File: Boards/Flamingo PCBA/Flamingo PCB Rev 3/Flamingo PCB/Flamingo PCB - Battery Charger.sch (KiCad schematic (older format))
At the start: 13 parts, among them J301 Wire Switch Here, J302 JST PH Battery Connector

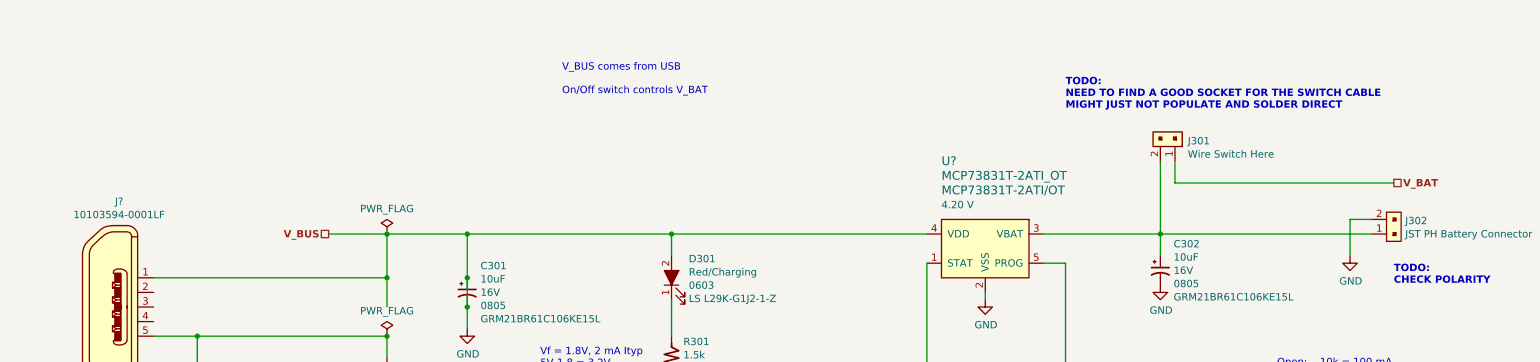
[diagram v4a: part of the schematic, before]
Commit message: NOSTUFF 5V LDO bc not needed. Added Sch diode on 5v LDO.
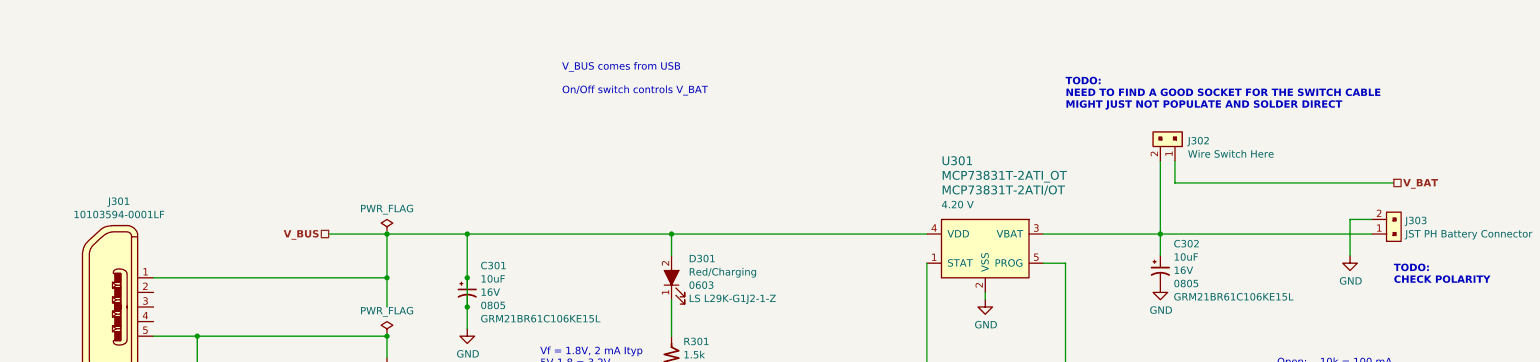
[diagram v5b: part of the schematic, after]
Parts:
- gave numbers to parts that had none: 2
- renumbered J301 to J302, J302 to J303
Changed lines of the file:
@@
 --------FLOW CHART--------\n\n###SHUTDOWN MODE\nVDD < VUVLO\nVDD < VBAT\nor\nPROG > 200 k\nSTAT = High Z\n\n###PRECONDITIONING \nCharge Current = IPREG\nSTAT = LOW\n\n###FAST CHARGE \nAlso get here if VBAT > VPTH from SHUTDOWN    \nor   \nVBAT < VRTH  from CHARGE COMPLETE\n\nCharge Current = IREG\nSTAT = LOW\n\n###CONSTANT VOLTAGE \nCharge Voltage = VREG\nSTAT = LOW\n\n###CHARGE MODE \nSTAT = HIGH (MCP73831)\nSTAT = High Z (MCP73832)\n\n--------PART NUMBER BREAKDOWN--------\n\nMCP73831T - 2 * * * _ OT\n\n(T) Tape and reel\n(2) 4.20 V regulated\n(OT) SMall Outline Transistor SOT23 T-Lead\n\n#######\n\nMCP73831T - 2 A C I _ OT\n(AT) Ipreg/Ireg = 10%\n        Iterm/Ireg = 7.5%\n\nMCP73831T - 2 A T I _ OT\n(AT) Ipreg/Ireg = 10%\n        Iterm/Ireg = 20%\n\nMCP73831T - 2 D C I _ OT\n(DC) Ipreg/Ireg = 100%\n        Iterm/Ireg = 7.5%
 $Comp
-L power:GND #PWR0303
+L power:GND #PWR0304
 U 1 1 5F7DD8CE
 P 7100 2700
-F 0 "#PWR0303" H 7100 2450 50  0001 C CNN
+F 0 "#PWR0304" H 7100 2450 50  0001 C CNN
 F 1 "GND" H 7105 2527 50  0000 C CNN
 F 2 "" H 7100 2700 50  0001 C CNN
@@
 $EndComp
 $Comp
-L power:GND #PWR0304
+L power:GND #PWR0305
 U 1 1 5F7E1F62
 P 7700 4000
-F 0 "#PWR0304" H 7700 3750 50  0001 C CNN
+F 0 "#PWR0305" H 7700 3750 50  0001 C CNN
 F 1 "GND" H 7705 3827 50  0000 C CNN
 F 2 "" H 7700 4000 50  0001 C CNN
@@
 $EndComp
 $Comp
-L power:GND #PWR0305
+L power:GND #PWR0306
 U 1 1 5F7E390B
 P 8300 2600
-F 0 "#PWR0305" H 8300 2350 50  0001 C CNN
+F 0 "#PWR0306" H 8300 2350 50  0001 C CNN
 F 1 "GND" H 8305 2427 50  0000 C CNN
 F 2 "" H 8300 2600 50  0001 C CNN
@@
 Connection ~ 8300 2250
 $Comp
-L power:GND #PWR0306
+L power:GND #PWR0307
 U 1 1 5F7E6098
 P 9600 2400
-F 0 "#PWR0306" H 9600 2150 50  0001 C CNN
+F 0 "#PWR0307" H 9600 2150 50  0001 C CNN
 F 1 "GND" H 9605 2227 50  0000 C CNN
 F 2 "" H 9600 2400 50  0001 C CNN
@@
 	7500 2450 7650 2450
 $Comp
-L power:GND #PWR0301
+L power:GND #PWR0302
 U 1 1 5F7ED2F5
 P 3550 2900
-F 0 "#PWR0301" H 3550 2650 50  0001 C CNN
+F 0 "#PWR0302" H 3550 2650 50  0001 C CNN
 F 1 "GND" H 3555 2727 50  0000 C CNN
 F 2 "" H 3550 2900 50  0001 C CNN
@@
 	4950 4500 4950 4700
 $Comp
-L power:GND #PWR0302
+L power:GND #PWR0303
 U 1 1 5F7EC089
 P 4950 4700
-F 0 "#PWR0302" H 4950 4450 50  0001 C CNN
+F 0 "#PWR0303" H 4950 4450 50  0001 C CNN
 F 1 "GND" H 4955 4527 50  0000 C CNN
 F 2 "" H 4950 4700 50  0001 C CNN
@@
 TODO:\nNEED TO FIND A GOOD SOCKET FOR THE SWITCH CABLE\nMIGHT JUST NOT POPULATE AND SOLDER DIRECT
 $Comp
-L dk_Rectangular-Connectors-Headers-Male-Pins:S2B-PH-K-S_LF__SN_ J301
+L dk_Rectangular-Connectors-Headers-Male-Pins:S2B-PH-K-S_LF__SN_ J302
 U 1 1 5F82D9D3
 P 8400 1650
-F 0 "J301" H 8312 1612 50  0000 R CNN
+F 0 "J302" H 8312 1612 50  0000 R CNN
 F 1 "Wire Switch Here" H 8312 1703 50  0000 R CNN
 F 2 "digikey-footprints:PinHeader_1x2_P2mm_Drill1mm_RA" H 8600 1850 60  0001 L CNN
@@
 	8300 2250 9750 2250
 $Comp
-L dk_Rectangular-Connectors-Headers-Male-Pins:S2B-PH-K-S_LF__SN_ J302
+L dk_Rectangular-Connectors-Headers-Male-Pins:S2B-PH-K-S_LF__SN_ J303
 U 1 1 5F8290D6
 P 9850 2250
-F 0 "J302" V 9941 2122 50  0000 R CNN
+F 0 "J303" V 9941 2122 50  0000 R CNN
 F 1 "JST PH Battery Connector" V 9850 2122 50  0000 R CNN
 F 2 "digikey-footprints:PinHeader_1x2_P2mm_Drill1mm_RA" H 10050 2450 60  0001 L CNN
@@
 	7650 3150 8150 3150
 $Comp
-L dk_USB-DVI-HDMI-Connectors:10103594-0001LF J?
+L dk_USB-DVI-HDMI-Connectors:10103594-0001LF J301
 U 1 1 5F8008FC
 P 1150 2750
-F 0 "J?" H 1164 3473 50  0000 C CNN
+F 0 "J301" H 1164 3473 50  0000 C CNN
 F 1 "10103594-0001LF" H 1164 3382 50  0000 C CNN
 F 2 "digikey-footprints:USB_Micro_B_Female_10103594-0001LF" H 1350 2950 60  0001 L CNN
@@
 Connection ~ 3000 2250
 $Comp
-L power:GND #PWR?
+L power:GND #PWR0301
 U 1 1 5F80F687
 P 3000 3100
-F 0 "#PWR?" H 3000 2850 50  0001 C CNN
+F 0 "#PWR0301" H 3000 2850 50  0001 C CNN
 F 1 "GND" H 3005 2927 50  0000 C CNN
 F 2 "" H 3000 3100 50  0001 C CNN
@@
 Will need to take some approach to negotiating higher power delivery if I am planning on using more than 500 mA. For example, a 2000 mAh LiPo charges at 1200 mA.\n\nApproaches are:\n\nDont.\nhttps://www.maximintegrated.com/en/design/technical-documents/tutorials/4/4803.html#3
 $Comp
-L power:PWR_FLAG #FLG?
+L power:PWR_FLAG #FLG0302
 U 1 1 5F810FFE
 P 3000 2950
-F 0 "#FLG?" H 3000 3025 50  0001 C CNN
+F 0 "#FLG0302" H 3000 3025 50  0001 C CNN
 F 1 "PWR_FLAG" H 3000 3123 50  0000 C CNN
 F 2 "" H 3000 2950 50  0001 C CNN
@@
 V_BUS comes from USB\n\nOn/Off switch controls V_BAT
 $Comp
-L MyICs:MCP73831T-2ATI_OT U?
+L MyICs:MCP73831T-2ATI_OT U301
 U 1 1 5F91A003
 P 7100 2250
-F 0 "U?" H 6800 2750 60  0000 L CNN
+F 0 "U301" H 6800 2750 60  0000 L CNN
 F 1 "MCP73831T-2ATI_OT" H 6800 2650 60  0000 L CNN
 F 2 "digikey-footprints:SOT-753" H 8000 2500 60  0001 L CNN

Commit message: Moved Battery Charger sheet into Power sheet
Right before addition of power sharing mosfet, maybe
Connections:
- wire segments 45 -> 44
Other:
- note added: "Will need to take some approach to negotiating higher power delivery\n if I am planning on using more than 500 mA. For example, \na 2000 mAh LiPo charges at 1200 mA.\n\nApproaches are:\n\nDont.\nhttps://www.maximintegrated.com/en/design/technical-documents/tutorials/4/4803.html#3"
- note added: "https://easyeda.com/gerdmuller.de/lithium-battery-charger-mcp73831-with-load-sharing"
- note added: "https://www.eevblog.com/forum/microcontrollers/rechargeable-battery-solution-for-mcu-projects/msg630455/#msg630455"
- note added: "independent of the capacitor’s minimum\nEffective Series Resistance (ESR) value. The actual\nvalue of the capacitor (and its associated ESR)\ndepends on the output load current. A 4.7 µF ceramic,\ntantalum or aluminum electrolytic capacitor at the\noutput is usually sufficient to ensure stability for output\ncurrents up to a 500 mA."
- note removed: "Will need to take some approach to negotiating higher power delivery if I am planning on using more than 500 mA. For example, a 2000 mAh LiPo charges at 1200 mA.\n\nApproaches are:\n\nDont.\nhttps://www.maximintegrated.com/en/design/technical-documents/tutorials/4/4803.html#3"
